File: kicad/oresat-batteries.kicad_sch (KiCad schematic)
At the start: 0 parts

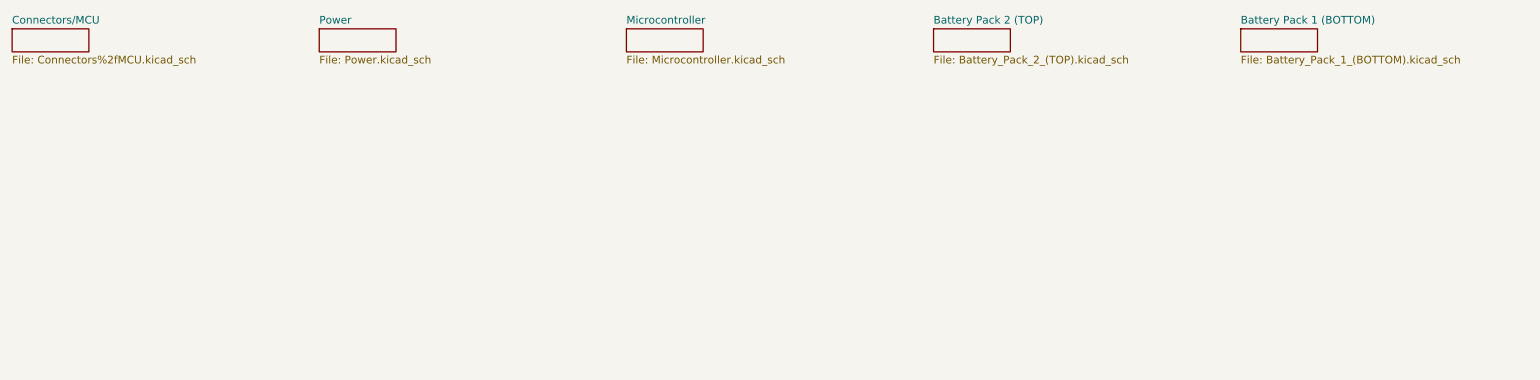
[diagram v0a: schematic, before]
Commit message: Updating KiCAD import of EAGLE battery card v3.0 and calling it v3.1 because the gerber files will definitely be different and we'll probably implement a few small changes. Reimports, renames, and fixes .gitignore file. Oh and makes the worksheets pretty.
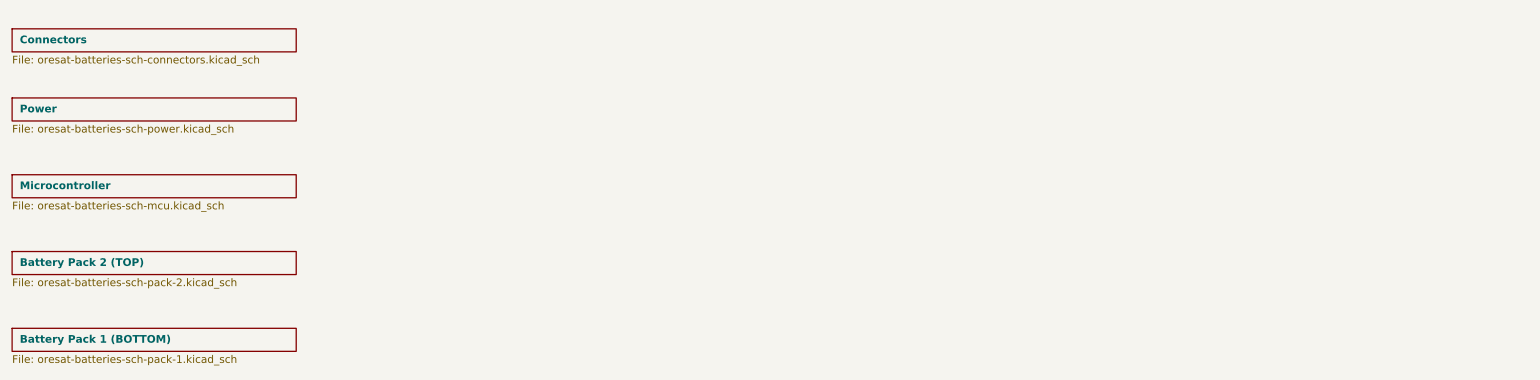
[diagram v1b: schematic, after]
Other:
- sheet Connectors/MCU renamed Connectors
- sheet Battery Pack 1 (BOTTOM): file Battery_Pack_1_(BOTTOM).kicad_sch -> oresat-batteries-sch-pack-1.kicad_sch
- sheet Battery Pack 2 (TOP): file Battery_Pack_2_(TOP).kicad_sch -> oresat-batteries-sch-pack-2.kicad_sch
- sheet Connectors: file Connectors%2fMCU.kicad_sch -> oresat-batteries-sch-connectors.kicad_sch
- sheet Microcontroller: file Microcontroller.kicad_sch -> oresat-batteries-sch-mcu.kicad_sch
- sheet Power: file Power.kicad_sch -> oresat-batteries-sch-power.kicad_sch
- title: (none) -> OreSat Battery Card
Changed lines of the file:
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@@
 (kicad_sch (version 20230121) (generator eeschema)
-  (paper "A4")
-  (sheet (at 127 25.4) (size 12.7 3.81) (fields_autoplaced)
+  (paper "B")
+  (title_block
+    (title "OreSat Battery Card")
+    (date "2023-12-02")
+    (rev "3.1")
+  )
+  (sheet (at 25.4 49.53) (size 46.99 3.81)
     (stroke (width 0) (type solid))
     (fill (color 0 0 0 0.0000))
-    (property "Sheetname" "Microcontroller" (at 127 24.6884 0)
-      (effects (font (size 1.27 1.27)) (justify left bottom))
+    (property "Sheetname" "Microcontroller" (at 26.67 52.07 0)
+      (effects (font (size 1.27 1.27) bold) (justify left bottom))
     )
-    (property "Sheetfile" "Microcontroller.kicad_sch" (at 127 29.7946 0)
+    (property "Sheetfile" "oresat-batteries-sch-mcu.kicad_sch" (at 25.4 53.9246 0)
       (effects (font (size 1.27 1.27)) (justify left top))
     )
@@
     )
   )
-  (sheet (at 25.4 25.4) (size 12.7 3.81) (fields_autoplaced)
+  (sheet (at 25.4 25.4) (size 46.99 3.81)
     (stroke (width 0) (type solid))
     (fill (color 0 0 0 0.0000))
-    (property "Sheetname" "Connectors/MCU" (at 25.4 24.6884 0)
-      (effects (font (size 1.27 1.27)) (justify left bottom))
+    (property "Sheetname" "Connectors" (at 26.67 27.94 0)
+      (effects (font (size 1.27 1.27) bold) (justify left bottom))
     )
-    (property "Sheetfile" "Connectors%2fMCU.kicad_sch" (at 25.4 29.7946 0)
+    (property "Sheetfile" "oresat-batteries-sch-connectors.kicad_sch" (at 25.4 29.7946 0)
       (effects (font (size 1.27 1.27)) (justify left top))
     )
@@
     )
   )
-  (sheet (at 228.6 25.4) (size 12.7 3.81) (fields_autoplaced)
+  (sheet (at 25.4 74.93) (size 46.99 3.81)
     (stroke (width 0) (type solid))
     (fill (color 0 0 0 0.0000))
-    (property "Sheetname" "Battery Pack 1 (BOTTOM)" (at 228.6 24.6884 0)
-      (effects (font (size 1.27 1.27)) (justify left bottom))
+    (property "Sheetname" "Battery Pack 1 (BOTTOM)" (at 26.67 77.47 0)
+      (effects (font (size 1.27 1.27) bold) (justify left bottom))
     )
-    (property "Sheetfile" "Battery_Pack_1_(BOTTOM).kicad_sch" (at 228.6 29.7946 0)
+    (property "Sheetfile" "oresat-batteries-sch-pack-1.kicad_sch" (at 25.4 79.3246 0)
       (effects (font (size 1.27 1.27)) (justify left top))
     )
@@
     )
   )
-  (sheet (at 76.2 25.4) (size 12.7 3.81) (fields_autoplaced)
+  (sheet (at 25.4 36.83) (size 46.99 3.81)
     (stroke (width 0) (type solid))
     (fill (color 0 0 0 0.0000))
-    (property "Sheetname" "Power" (at 76.2 24.6884 0)
-      (effects (font (size 1.27 1.27)) (justify left bottom))
+    (property "Sheetname" "Power" (at 26.67 39.37 0)
+      (effects (font (size 1.27 1.27) bold) (justify left bottom))
     )
-    (property "Sheetfile" "Power.kicad_sch" (at 76.2 29.7946 0)
+    (property "Sheetfile" "oresat-batteries-sch-power.kicad_sch" (at 25.4 41.2246 0)
       (effects (font (size 1.27 1.27)) (justify left top))
     )
@@
     )
   )
-  (sheet (at 177.8 25.4) (size 12.7 3.81) (fields_autoplaced)
+  (sheet (at 25.4 62.23) (size 46.99 3.81)
     (stroke (width 0) (type solid))
     (fill (color 0 0 0 0.0000))
-    (property "Sheetname" "Battery Pack 2 (TOP)" (at 177.8 24.6884 0)
-      (effects (font (size 1.27 1.27)) (justify left bottom))
+    (property "Sheetname" "Battery Pack 2 (TOP)" (at 26.67 64.77 0)
+      (effects (font (size 1.27 1.27) bold) (justify left bottom))
     )
-    (property "Sheetfile" "Battery_Pack_2_(TOP).kicad_sch" (at 177.8 29.7946 0)
+    (property "Sheetfile" "oresat-batteries-sch-pack-2.kicad_sch" (at 25.4 66.6246 0)
       (effects (font (size 1.27 1.27)) (justify left top))
     )

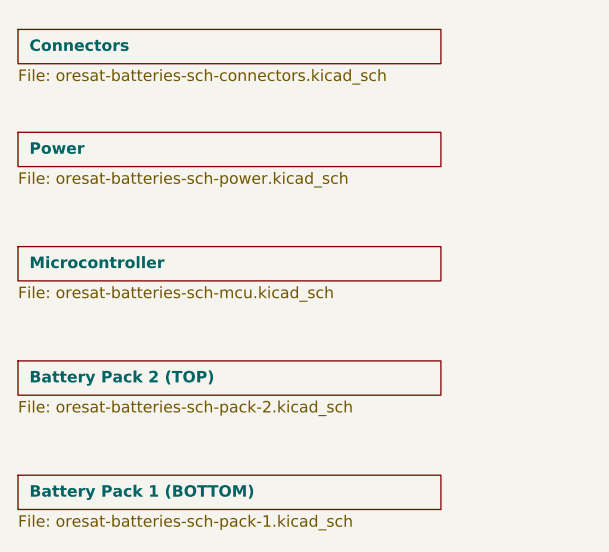
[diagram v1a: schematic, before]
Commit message: Kicad import try #3. Now with DXFs from custom EAGLE layers. Schematic worksheets and names updated.
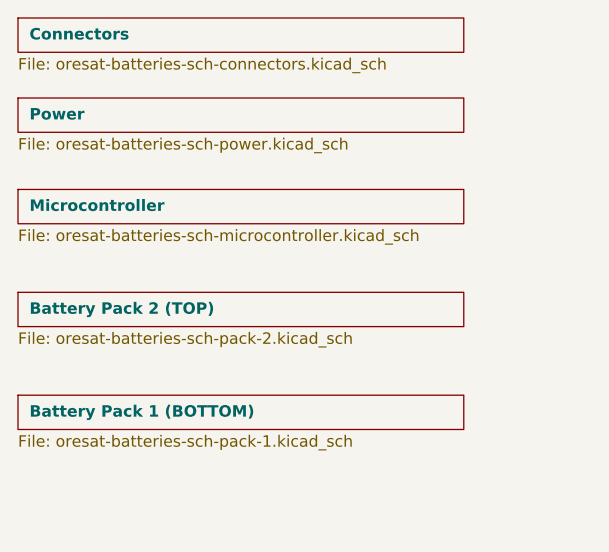
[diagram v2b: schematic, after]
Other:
- sheet Microcontroller: file oresat-batteries-sch-mcu.kicad_sch -> oresat-batteries-sch-microcontroller.kicad_sch
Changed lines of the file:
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@@
     (rev "3.1")
   )
-  (sheet (at 25.4 49.53) (size 46.99 3.81)
+  (sheet (at 25.4 43.18) (size 49.53 3.81)
     (stroke (width 0) (type solid))
     (fill (color 0 0 0 0.0000))
-    (property "Sheetname" "Microcontroller" (at 26.67 52.07 0)
+    (property "Sheetname" "Microcontroller" (at 26.67 45.72 0)
       (effects (font (size 1.27 1.27) bold) (justify left bottom))
     )
-    (property "Sheetfile" "oresat-batteries-sch-mcu.kicad_sch" (at 25.4 53.9246 0)
+    (property "Sheetfile" "oresat-batteries-sch-microcontroller.kicad_sch" (at 25.4 47.5746 0)
       (effects (font (size 1.27 1.27)) (justify left top))
     )
     (instances
       (project "oresat-batteries"
-        (path "/3521a840-1323-4632-a472-140474b47f95" (page "3"))
+        (path "/d5070776-2522-4f7b-9d31-10770161e48a" (page "3"))
       )
     )
   )
-  (sheet (at 25.4 25.4) (size 46.99 3.81)
+  (sheet (at 25.4 54.61) (size 49.53 3.81)
     (stroke (width 0) (type solid))
     (fill (color 0 0 0 0.0000))
-    (property "Sheetname" "Connectors" (at 26.67 27.94 0)
+    (property "Sheetname" "Battery Pack 2 (TOP)" (at 26.67 57.15 0)
       (effects (font (size 1.27 1.27) bold) (justify left bottom))
     )
-    (property "Sheetfile" "oresat-batteries-sch-connectors.kicad_sch" (at 25.4 29.7946 0)
+    (property "Sheetfile" "oresat-batteries-sch-pack-2.kicad_sch" (at 25.4 59.0046 0)
       (effects (font (size 1.27 1.27)) (justify left top))
     )
     (instances
       (project "oresat-batteries"
-        (path "/3521a840-1323-4632-a472-140474b47f95" (page "1"))
+        (path "/d5070776-2522-4f7b-9d31-10770161e48a" (page "4"))
       )
     )
   )
-  (sheet (at 25.4 74.93) (size 46.99 3.81)
+  (sheet (at 25.4 66.04) (size 49.53 3.81)
     (stroke (width 0) (type solid))
     (fill (color 0 0 0 0.0000))
-    (property "Sheetname" "Battery Pack 1 (BOTTOM)" (at 26.67 77.47 0)
+    (property "Sheetname" "Battery Pack 1 (BOTTOM)" (at 26.67 68.58 0)
       (effects (font (size 1.27 1.27) bold) (justify left bottom))
     )
-    (property "Sheetfile" "oresat-batteries-sch-pack-1.kicad_sch" (at 25.4 79.3246 0)
+    (property "Sheetfile" "oresat-batteries-sch-pack-1.kicad_sch" (at 25.4 70.4346 0)
       (effects (font (size 1.27 1.27)) (justify left top))
     )
     (instances
       (project "oresat-batteries"
-        (path "/3521a840-1323-4632-a472-140474b47f95" (page "5"))
+        (path "/d5070776-2522-4f7b-9d31-10770161e48a" (page "5"))
       )
     )
   )
-  (sheet (at 25.4 36.83) (size 46.99 3.81)
+  (sheet (at 25.4 33.02) (size 49.53 3.81)
     (stroke (width 0) (type solid))
     (fill (color 0 0 0 0.0000))
-    (property "Sheetname" "Power" (at 26.67 39.37 0)
+    (property "Sheetname" "Power" (at 26.67 35.56 0)
       (effects (font (size 1.27 1.27) bold) (justify left bottom))
     )
-    (property "Sheetfile" "oresat-batteries-sch-power.kicad_sch" (at 25.4 41.2246 0)
+    (property "Sheetfile" "oresat-batteries-sch-power.kicad_sch" (at 25.4 37.4146 0)
       (effects (font (size 1.27 1.27)) (justify left top))
     )
     (instances
       (project "oresat-batteries"
-        (path "/3521a840-1323-4632-a472-140474b47f95" (page "2"))
+        (path "/d5070776-2522-4f7b-9d31-10770161e48a" (page "2"))
       )
     )
   )
-  (sheet (at 25.4 62.23) (size 46.99 3.81)
+  (sheet (at 25.4 24.13) (size 49.53 3.81)
     (stroke (width 0) (type solid))
     (fill (color 0 0 0 0.0000))
-    (property "Sheetname" "Battery Pack 2 (TOP)" (at 26.67 64.77 0)
+    (property "Sheetname" "Connectors" (at 26.67 26.67 0)
       (effects (font (size 1.27 1.27) bold) (justify left bottom))
     )
-    (property "Sheetfile" "oresat-batteries-sch-pack-2.kicad_sch" (at 25.4 66.6246 0)
+    (property "Sheetfile" "oresat-batteries-sch-connectors.kicad_sch" (at 25.4 28.5246 0)
       (effects (font (size 1.27 1.27)) (justify left top))
     )
     (instances
       (project "oresat-batteries"
-        (path "/3521a840-1323-4632-a472-140474b47f95" (page "4"))
+        (path "/d5070776-2522-4f7b-9d31-10770161e48a" (page "1"))
       )
     )

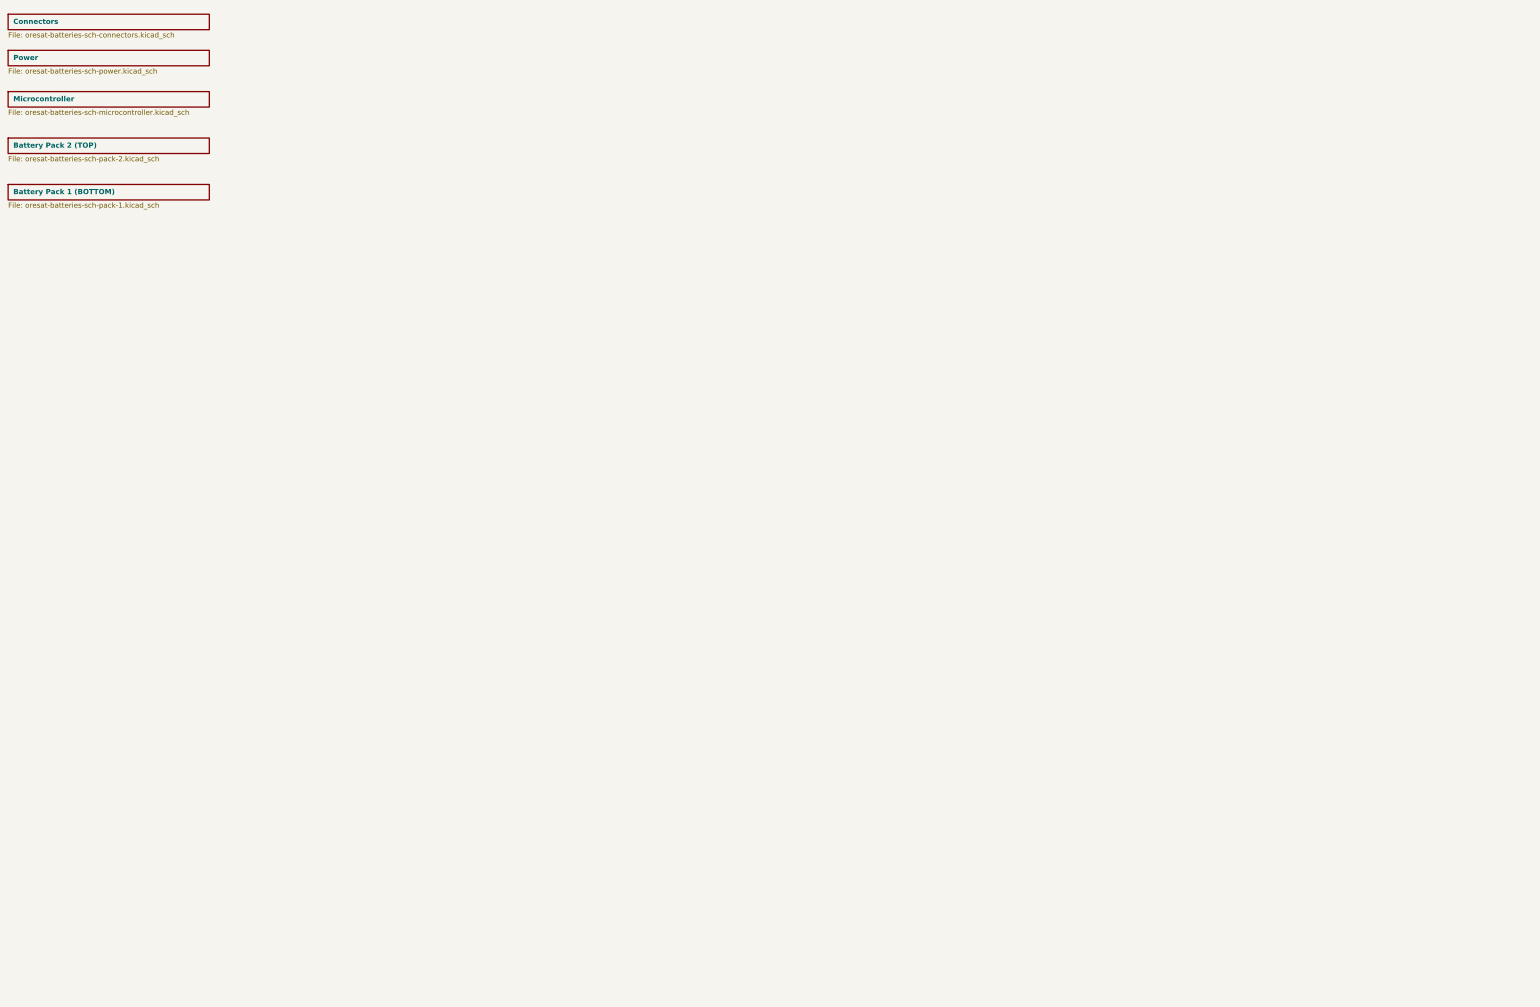
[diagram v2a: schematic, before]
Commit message: Starting Battery Card 4.0
Changed root sheet to hierarchical sheet. No change to schematic or layout yet. Updated the stackup with oresat template. Switched to variables for version and date.
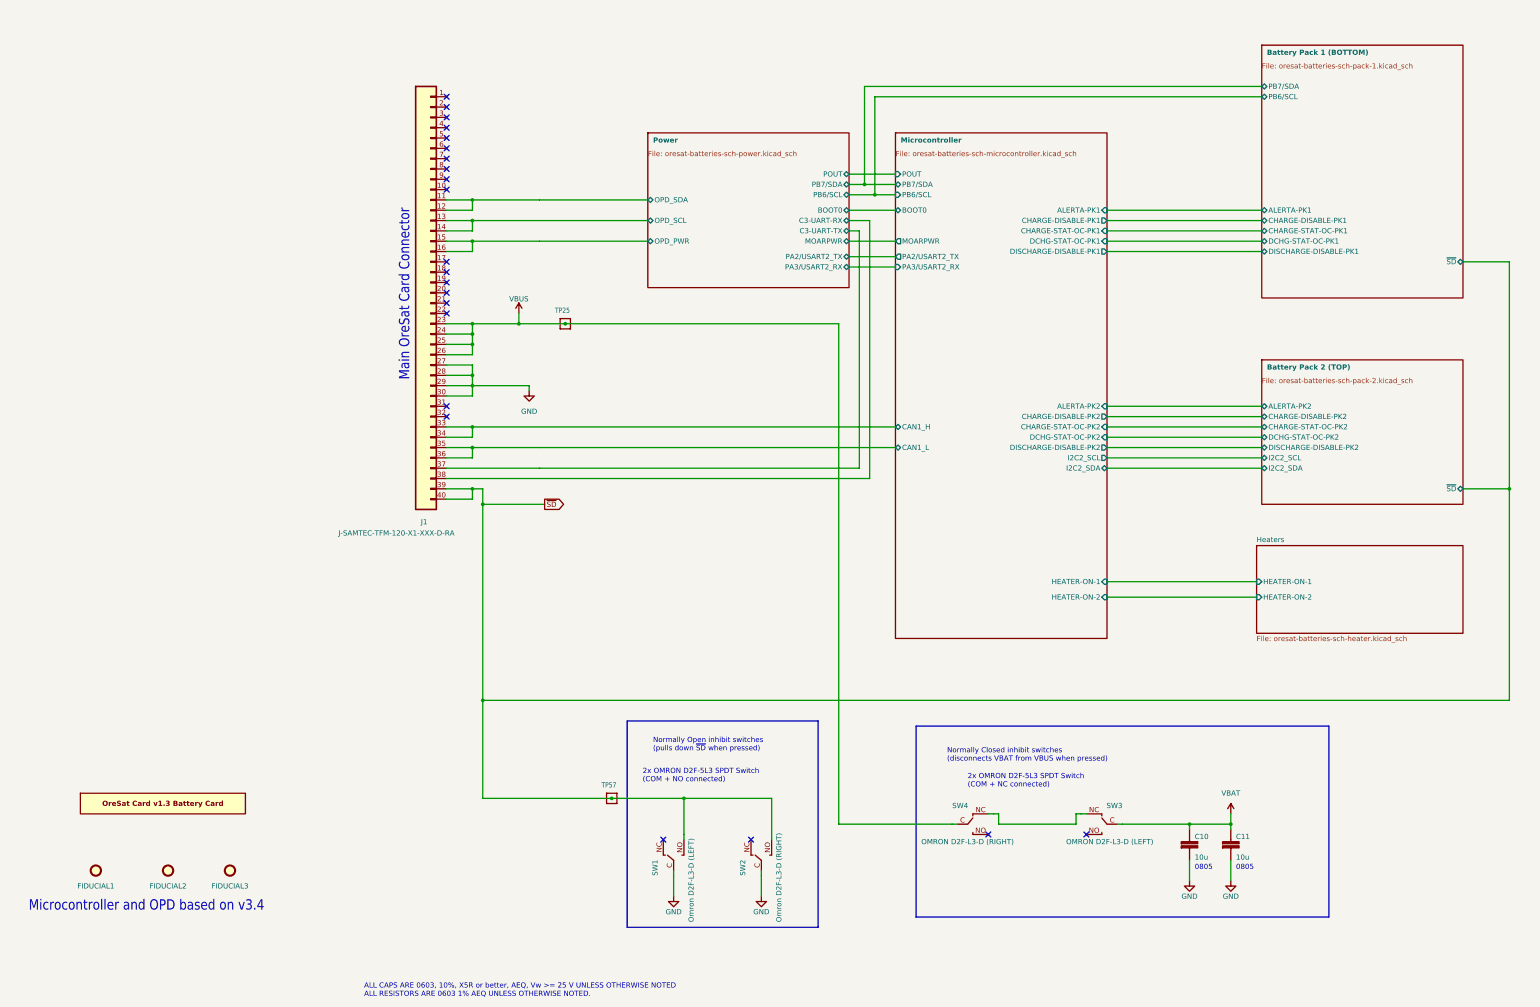
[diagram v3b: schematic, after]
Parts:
- added C10, C11: 10u, oresat-batteries:.0805-B-NOSILK, symbol oresat-batteries-eagle-import:C-EU0805-B-NOSILK
- added FIDUCIAL1, FIDUCIAL2, FIDUCIAL3: FIDUCIAL-1.0X2.0, Fiducial:Fiducial_1mm_Mask2mm, symbol Mechanical:Fiducial
- added J1: J-SAMTEC-TFM-120-X1-XXX-D-RA, oresat-connectors:J-SAMTEC-TFM-120-X1-XXX-D-RA, symbol oresat-connectors:J-SAMTEC-TFM-120-01-L-D-RA
- added PCB1: ORESAT-CARD-V1.3-BATTERY, oresat-pcbs:ORESAT-CARD-V1.3-BATTERY-V3.0, symbol oresat-pcbs:ORESAT-CARD-V1.3-BATTERY
- added SW1: Omron D2F-L3-D (LEFT), oresat-misc:D2F-L3-D-HORIZONTAL-L, symbol oresat-misc:OMRON-D2F-L3-D-LEFT
- added SW2: Omron D2F-L3-D (RIGHT), oresat-misc:D2F-L3-D-HORIZONTAL-R, symbol oresat-misc:OMRON-D2F-L3-D-RIGHT
- added SW3: OMRON D2F-L3-D (LEFT), oresat-misc:D2F-L3-D-HORIZONTAL-L, symbol oresat-misc:OMRON-D2F-L3-D-LEFT
- added SW4: OMRON D2F-L3-D (RIGHT), oresat-misc:D2F-L3-D-HORIZONTAL-R, symbol oresat-misc:OMRON-D2F-L3-D-RIGHT
- added TP25, TP57: TEST-POINT-LARGE-SQUARE, oresat-batteries:1X01, symbol oresat-batteries-eagle-import:TEST-POINT-LARGE-SQUARE
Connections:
- new net: SW3.NC, SW4.NC
- new net GND: C10.2, C11.2, J1.27, J1.28, J1.29, J1.30, SW1.C (COM), SW2.C (COM)
- new net Microcontroller/CAN1_H: J1.33, J1.34
- new net Microcontroller/CAN1_L: J1.35, J1.36
- new net Power/C3-UART-RX: J1.38
- new net Power/C3-UART-TX: J1.37
- new net Power/OPD_PWR: J1.15, J1.16
- new net Power/OPD_SCL: J1.13, J1.14
- new net Power/OPD_SDA: J1.11, J1.12
- new net VBAT: C10.1, C11.1, SW3.C (COM)
- new net VBUS: J1.23, J1.24, J1.25, J1.26, SW4.C (COM), TP25.1
- new net ~{SD}: J1.39, J1.40, SW1.NO, SW2.NO, TP57.1
- no-connect marks 0 -> 22
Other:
- removed sheet Connectors
- added sheet Heaters (oresat-batteries-sch-heater.kicad_sch)
- sheet Battery Pack 1 (BOTTOM) ports: added ALERTA-PK1, CHARGE-DISABLE-PK1, CHARGE-STAT-OC-PK1, DCHG-STAT-OC-PK1, DISCHARGE-DISABLE-PK1, PB6/SCL, PB7/SDA, ~{SD}; removed none
- sheet Battery Pack 2 (TOP) ports: added ALERTA-PK2, CHARGE-DISABLE-PK2, CHARGE-STAT-OC-PK2, DCHG-STAT-OC-PK2, DISCHARGE-DISABLE-PK2, I2C2_SCL, I2C2_SDA, ~{SD}; removed none
- sheet Microcontroller ports: added ALERTA-PK1, ALERTA-PK2, BOOT0, CAN1_H, CAN1_L, CHARGE-DISABLE-PK1, CHARGE-DISABLE-PK2, CHARGE-STAT-OC-PK1, CHARGE-STAT-OC-PK2, DCHG-STAT-OC-PK1, DCHG-STAT-OC-PK2, DISCHARGE-DISABLE-PK1, DISCHARGE-DISABLE-PK2, HEATER-ON-1, HEATER-ON-2, I2C2_SCL, I2C2_SDA, MOARPWR, PA2/USART2_TX, PA3/USART2_RX, PB6/SCL, PB7/SDA, POUT; removed none
- sheet Power ports: added BOOT0, C3-UART-RX, C3-UART-TX, MOARPWR, OPD_PWR, OPD_SCL, OPD_SDA, PA2/USART2_TX, PA3/USART2_RX, PB6/SCL, PB7/SDA, POUT; removed none
- note added: "0805"
- note added: "2x OMRON D2F-5L3 SPDT Switch (COM + NC connected)"
- note added: "2x OMRON D2F-5L3 SPDT Switch (COM + NO connected)"
- note added: "ALL CAPS ARE 0603, 10%, X5R or better, AEQ, Vw >= 25 V UNLESS OTHERWISE NOTED ALL RESISTORS ARE 0603 1% AEQ UNLESS OTHERWISE NOTED."
- note added: "Main OreSat Card Connector"
- note added: "Microcontroller and OPD based on v3.4"
- note added: "Normally Closed inhibit switches (disconnects VBAT from VBUS when pressed)"
- note added: "Normally Open inhibit switches (pulls down ~{SD} when pressed)"
- company: (none) -> Portland State Aerospace Society
